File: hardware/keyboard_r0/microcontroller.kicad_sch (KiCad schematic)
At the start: 29 parts

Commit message: Remaining schematic updates from 8.0 migration.
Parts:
- SWT1: symbol Switch:SW_SPDT -> mass:SW_SPDT
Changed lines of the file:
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@@
 	)
 	(junction
-		(at 243.84 121.92)
-		(diameter 0)
-		(color 0 0 0 0)
-	)
-	(junction
 		(at 182.88 132.08)
 		(diameter 0)
@@
 	)
 	(junction
+		(at 243.84 121.92)
+		(diameter 0)
+		(color 0 0 0 0)
+	)
+	(junction
 		(at 160.02 149.86)
 		(diameter 0)
@@
 	(wire
 		(pts
-			(xy 243.84 121.92) (xy 246.38 121.92)
-		)
-		(stroke
-			(width 0)
-			(type default)
-		)
-	)
-	(wire
-		(pts
 			(xy 172.72 154.94) (xy 172.72 157.48)
 		)
@@
 	(wire
 		(pts
+			(xy 243.84 121.92) (xy 246.38 121.92)
+		)
+		(stroke
+			(width 0)
+			(type default)
+		)
+	)
+	(wire
+		(pts
 			(xy 73.66 101.6) (xy 78.74 101.6)
 		)
@@
 	)
 	(symbol
+		(lib_id "power:PWR_FLAG")
+		(at 246.38 121.92 270)
+		(unit 1)
+		(exclude_from_sim no)
+		(in_bom yes)
+		(on_board yes)
+		(dnp no)
+		(fields_autoplaced yes)
+		(property "Reference" "#FLG010"
+			(at 248.285 121.92 0)
+			(effects
+				(font
+					(size 1.27 1.27)
+				)
+				(hide yes)
+			)
+		)
+		(property "Value" "PWR_FLAG"
+			(at 250.19 121.9199 90)
+			(effects
+				(font
+					(size 1.27 1.27)
+				)
+				(justify left)
+			)
+		)
+		(property "Footprint" ""
+			(at 246.38 121.92 0)
+			(effects
+				(font
+					(size 1.27 1.27)
+				)
+				(hide yes)
+			)
+		)
+		(property "Datasheet" "~"
+			(at 246.38 121.92 0)
+			(effects
+				(font
+					(size 1.27 1.27)
+				)
+				(hide yes)
+			)
+		)
+		(property "Description" "Special symbol for telling ERC where power comes from"
+			(at 246.38 121.92 0)
+			(effects
+				(font
+					(size 1.27 1.27)
+				)
+				(hide yes)
+			)
+		)
+		(pin "1"
+		)
+		(instances
+			(project ""
+				(path "/91af5a4b-5f23-44d6-90d8-0a04513e8c93/41b52e08-2c8b-489c-8351-03e2c976897f"
+					(reference "#FLG010")
+					(unit 1)
+				)
+				(path "/91af5a4b-5f23-44d6-90d8-0a04513e8c93/a6bdd940-be59-4885-8b20-083045d4e03a"
+					(reference "#FLG011")
+					(unit 1)
+				)
+			)
+		)
+	)
+	(symbol
 		(lib_id "Device:C")
 		(at 91.44 95.25 0)
@@
 		)
 		(property "Value" "PWR_FLAG"
-			(at 241.3 83.82 0)
+			(at 241.3 82.55 0)
 			(effects
 				(font
 					(size 1.27 1.27)
 				)
-				(justify bottom)
 			)
 		)
@@
 			)
 		)
-		(property "Description" ""
+		(property "Description" "Special symbol for telling ERC where power comes from"
 			(at 241.3 86.36 0)
 			(effects
@@
 			)
 		)
-		(property "Description" ""
+		(property "Description" "Power symbol creates a global label with name \"GND\" , ground"
 			(at 172.72 109.22 0)
 			(effects
@@
 			)
 		)
-		(property "Description" ""
+		(property "Description" "Power symbol creates a global label with name \"GND\" , ground"
 			(at 78.74 104.14 0)
 			(effects
@@
 			)
 		)
-		(property "Description" ""
+		(property "Description" "Power symbol creates a global label with name \"GND\" , ground"
 			(at 91.44 162.56 0)
 			(effects
@@
 		(fields_autoplaced yes)
 		(property "Reference" "BTT1"
-			(at 247.65 110.9979 0)
+			(at 247.65 111.1884 0)
 			(effects
 				(font
@@
 		)
 		(property "Value" "CR2032"
-			(at 247.65 113.5379 0)
+			(at 247.65 113.7284 0)
 			(effects
 				(font
@@
 			)
 		)
-		(property "Description" ""
+		(property "Description" "Power symbol creates a global label with name \"GND\" , ground"
 			(at 241.3 127 0)
 			(effects
@@
 			)
 		)
-		(property "Description" ""
+		(property "Description" "Power symbol creates a global label with name \"GND\" , ground"
 			(at 40.64 127 0)
 			(effects
@@
 			)
 		)
-		(property "Description" ""
+		(property "Description" "Power symbol creates a global label with name \"GND\" , ground"
 			(at 101.6 71.12 0)
 			(effects
@@
 	)
 	(symbol
-		(lib_id "Switch:SW_SPDT")
+		(lib_id "mass:SW_SPDT")
 		(at 241.3 99.06 90)
 		(mirror x)
@@
 			)
 		)
-		(property "Description" ""
+		(property "Description" "Power symbol creates a global label with name \"GND\" , ground"
 			(at 124.46 165.1 0)
 			(effects
@@
 	)
 	(symbol
-		(lib_id "power:PWR_FLAG")
-		(at 246.38 121.92 270)
-		(unit 1)
-		(exclude_from_sim no)
-		(in_bom yes)
-		(on_board yes)
-		(dnp no)
-		(property "Reference" "#FLG0103"
-			(at 248.285 121.92 0)
-			(effects
-				(font
-					(size 1.27 1.27)
-				)
-				(hide yes)
-			)
-		)
-		(property "Value" "PWR_FLAG"
-			(at 248.92 121.92 0)
-			(effects
-				(font
-					(size 1.27 1.27)
-				)
-				(justify bottom)
-			)
-		)
-		(property "Footprint" ""
-			(at 246.38 121.92 0)
-			(effects
-				(font
-					(size 1.27 1.27)
-				)
-				(hide yes)
-			)
-		)
-		(property "Datasheet" "~"
-			(at 246.38 121.92 0)
-			(effects
-				(font
-					(size 1.27 1.27)
-				)
-				(hide yes)
-			)
-		)
-		(property "Description" ""
-			(at 246.38 121.92 0)
-			(effects
-				(font
-					(size 1.27 1.27)
-				)
-				(hide yes)
-			)
-		)
-		(pin "1"
-		)
-		(instances
-			(project "ergodox_wireless_keyboard_r0"
-				(path "/91af5a4b-5f23-44d6-90d8-0a04513e8c93/41b52e08-2c8b-489c-8351-03e2c976897f"
-					(reference "#FLG0103")
-					(unit 1)
-				)
-				(path "/91af5a4b-5f23-44d6-90d8-0a04513e8c93/a6bdd940-be59-4885-8b20-083045d4e03a"
-					(reference "#FLG0104")
-					(unit 1)
-				)
-			)
-		)
-	)
-	(symbol
 		(lib_id "mass:nRF52820")
 		(at 139.7 106.68 0)
@@
 			)
 		)
-		(property "Description" ""
+		(property "Description" "Power symbol creates a global label with name \"GND\" , ground"
 			(at 198.12 104.14 0)
 			(effects
@@
 			)
 		)
-		(property "Description" ""
+		(property "Description" "Power symbol creates a global label with name \"GND\" , ground"
 			(at 195.58 134.62 0)
 			(effects

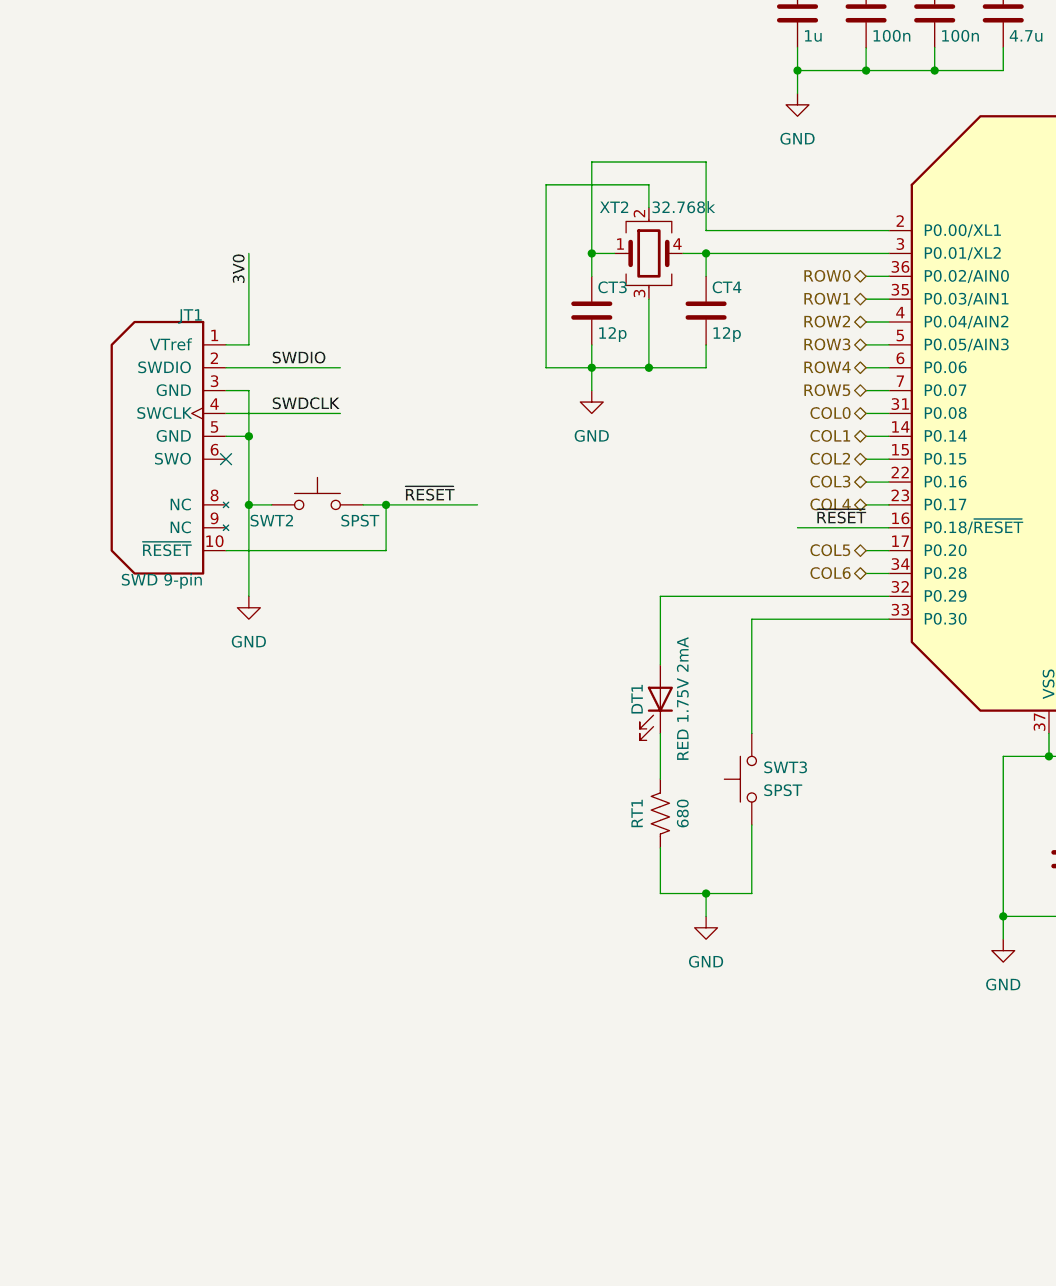
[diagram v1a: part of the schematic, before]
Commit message: Remove optional low-frequency oscillator circuit.
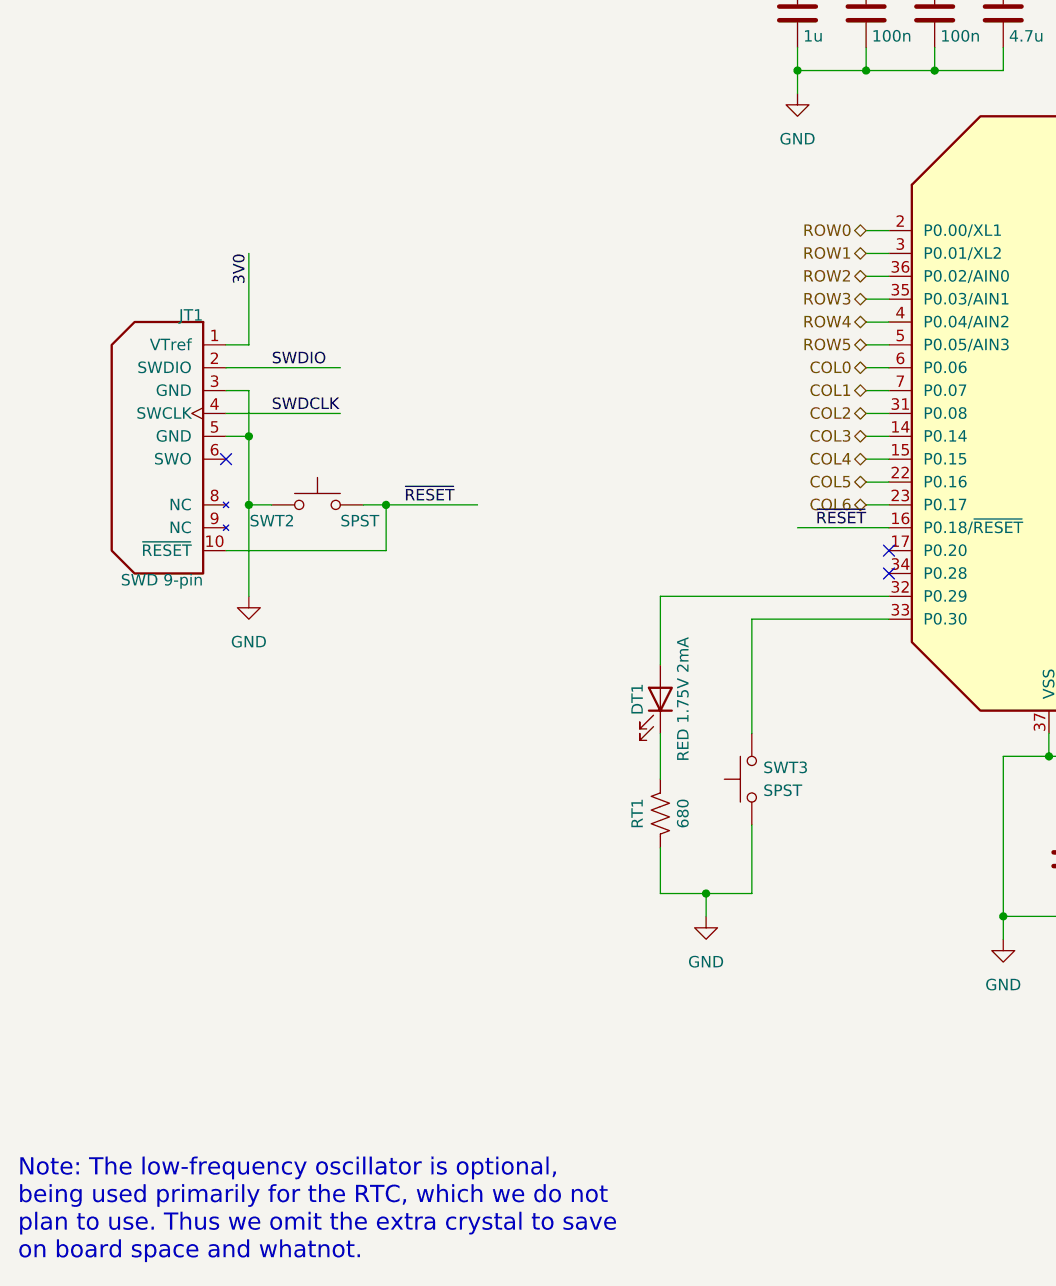
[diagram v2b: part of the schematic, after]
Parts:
- removed CT3, CT4: 12p, mass:0603, symbol Device:C
- removed XT2: 32.768k, mass:MC-146, symbol Device:Crystal_GND23
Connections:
- net COL0: now also UT1.6 (P0.06); no longer UT1.31 (P0.08)
- net COL1: now also UT1.7 (P0.07); no longer UT1.14 (P0.14)
- net COL2: now also UT1.31 (P0.08); no longer UT1.15 (P0.15)
- net COL3: now also UT1.14 (P0.14); no longer UT1.22 (P0.16)
- net COL4: now also UT1.15 (P0.15); no longer UT1.23 (P0.17)
- net COL5: now also UT1.22 (P0.16); no longer UT1.17 (P0.20)
- net COL6: now also UT1.23 (P0.17); no longer UT1.34 (P0.28)
- net ROW0: now also UT1.2 (P0.00/XL1); no longer UT1.36 (P0.02/AIN0)
- net ROW1: now also UT1.3 (P0.01/XL2); no longer UT1.35 (P0.03/AIN1)
- net ROW2: now also UT1.36 (P0.02/AIN0); no longer UT1.4 (P0.04/AIN2)
- net ROW3: now also UT1.35 (P0.03/AIN1); no longer UT1.5 (P0.05/AIN3)
- net ROW4: now also UT1.4 (P0.04/AIN2); no longer UT1.6 (P0.06)
- net ROW5: now also UT1.5 (P0.05/AIN3); no longer UT1.7 (P0.07)
- no-connect marks 5 -> 7
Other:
- note added: "Note: The low-frequency oscillator is optional, being used primarily for the RTC, which we do not plan to use. Thus we omit the extra crystal to save on board space and whatnot."

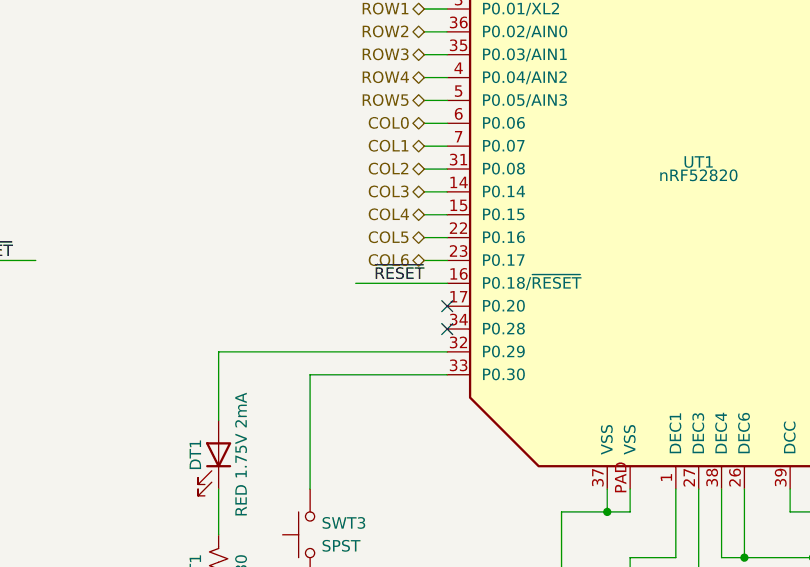
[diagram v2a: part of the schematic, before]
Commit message: Begin to route traces around the microcontroller.
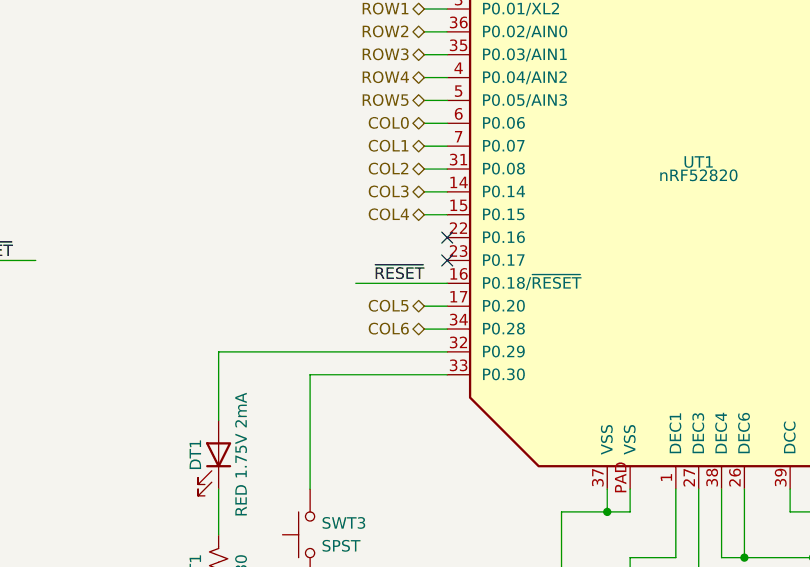
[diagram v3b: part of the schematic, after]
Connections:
- net COL5: now also UT1.17 (P0.20); no longer UT1.22 (P0.16)
- net COL6: now also UT1.34 (P0.28); no longer UT1.23 (P0.17)
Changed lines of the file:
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@@
-	)
-	(no_connect
-		(at 111.76 124.46)
 	)
 	(no_connect
@@
 	)
 	(no_connect
+		(at 111.76 114.3)
+	)
+	(no_connect
 		(at 167.64 114.3)
+	)
+	(no_connect
+		(at 111.76 116.84)
 	)
 	(no_connect
 		(at 167.64 109.22)
 	)
-	(no_connect
-		(at 111.76 121.92)
-	)
 	(wire
 		(pts
@@
 	(wire
 		(pts
-			(xy 109.22 116.84) (xy 111.76 116.84)
-		)
-		(stroke
-			(width 0)
-			(type default)
-		)
-	)
-	(wire
-		(pts
 			(xy 109.22 106.68) (xy 111.76 106.68)
 		)
@@
 	(wire
 		(pts
+			(xy 109.22 121.92) (xy 111.76 121.92)
+		)
+		(stroke
+			(width 0)
+			(type default)
+		)
+	)
+	(wire
+		(pts
 			(xy 167.64 101.6) (xy 177.8 101.6)
 		)
@@
 	(wire
 		(pts
+			(xy 109.22 124.46) (xy 111.76 124.46)
+		)
+		(stroke
+			(width 0)
+			(type default)
+		)
+	)
+	(wire
+		(pts
 			(xy 185.42 88.9) (xy 185.42 91.44)
 		)
@@
 		(pts
 			(xy 139.7 68.58) (xy 142.24 68.58)
-		)
-		(stroke
-			(width 0)
-			(type default)
-		)
-	)
-	(wire
-		(pts
-			(xy 109.22 114.3) (xy 111.76 114.3)
 		)
 		(stroke
@@
 		)
 	)
-	(hierarchical_label "COL6"
-		(shape bidirectional)
-		(at 109.22 116.84 180)
-		(fields_autoplaced yes)
-		(effects
-			(font
-				(size 1.27 1.27)
-			)
-			(justify right)
-		)
-	)
 	(hierarchical_label "COL3"
 		(shape bidirectional)
@@
 		)
 	)
+	(hierarchical_label "COL6"
+		(shape bidirectional)
+		(at 109.22 124.46 180)
+		(fields_autoplaced yes)
+		(effects
+			(font
+				(size 1.27 1.27)
+			)
+			(justify right)
+		)
+	)
 	(hierarchical_label "ROW5"
 		(shape bidirectional)
@@
 		)
 	)
-	(hierarchical_label "COL5"
-		(shape bidirectional)
-		(at 109.22 114.3 180)
-		(fields_autoplaced yes)
-		(effects
-			(font
-				(size 1.27 1.27)
-			)
-			(justify right)
-		)
-	)
 	(hierarchical_label "COL4"
 		(shape bidirectional)
@@
 		(fields_autoplaced yes)
 		(effects
+			(font
+				(size 1.27 1.27)
+			)
+			(justify right)
+		)
+	)
+	(hierarchical_label "COL5"
+		(shape bidirectional)
+		(at 109.22 121.92 180)
+		(fields_autoplaced yes)
+		(effects
